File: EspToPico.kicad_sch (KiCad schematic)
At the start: 16 parts, among them J1 Conn_01x20_Pin, J2 Conn_01x20_Pin, J3 USB_C_Receptacle_USB2.0_16P, U1 ESP32-WROOM-E, U2 AP2112K-3.3, U3 TPD3E001DRLR, U4 MCP2200-I-MQ, Y1 CSTNE12M0GH5L000R0

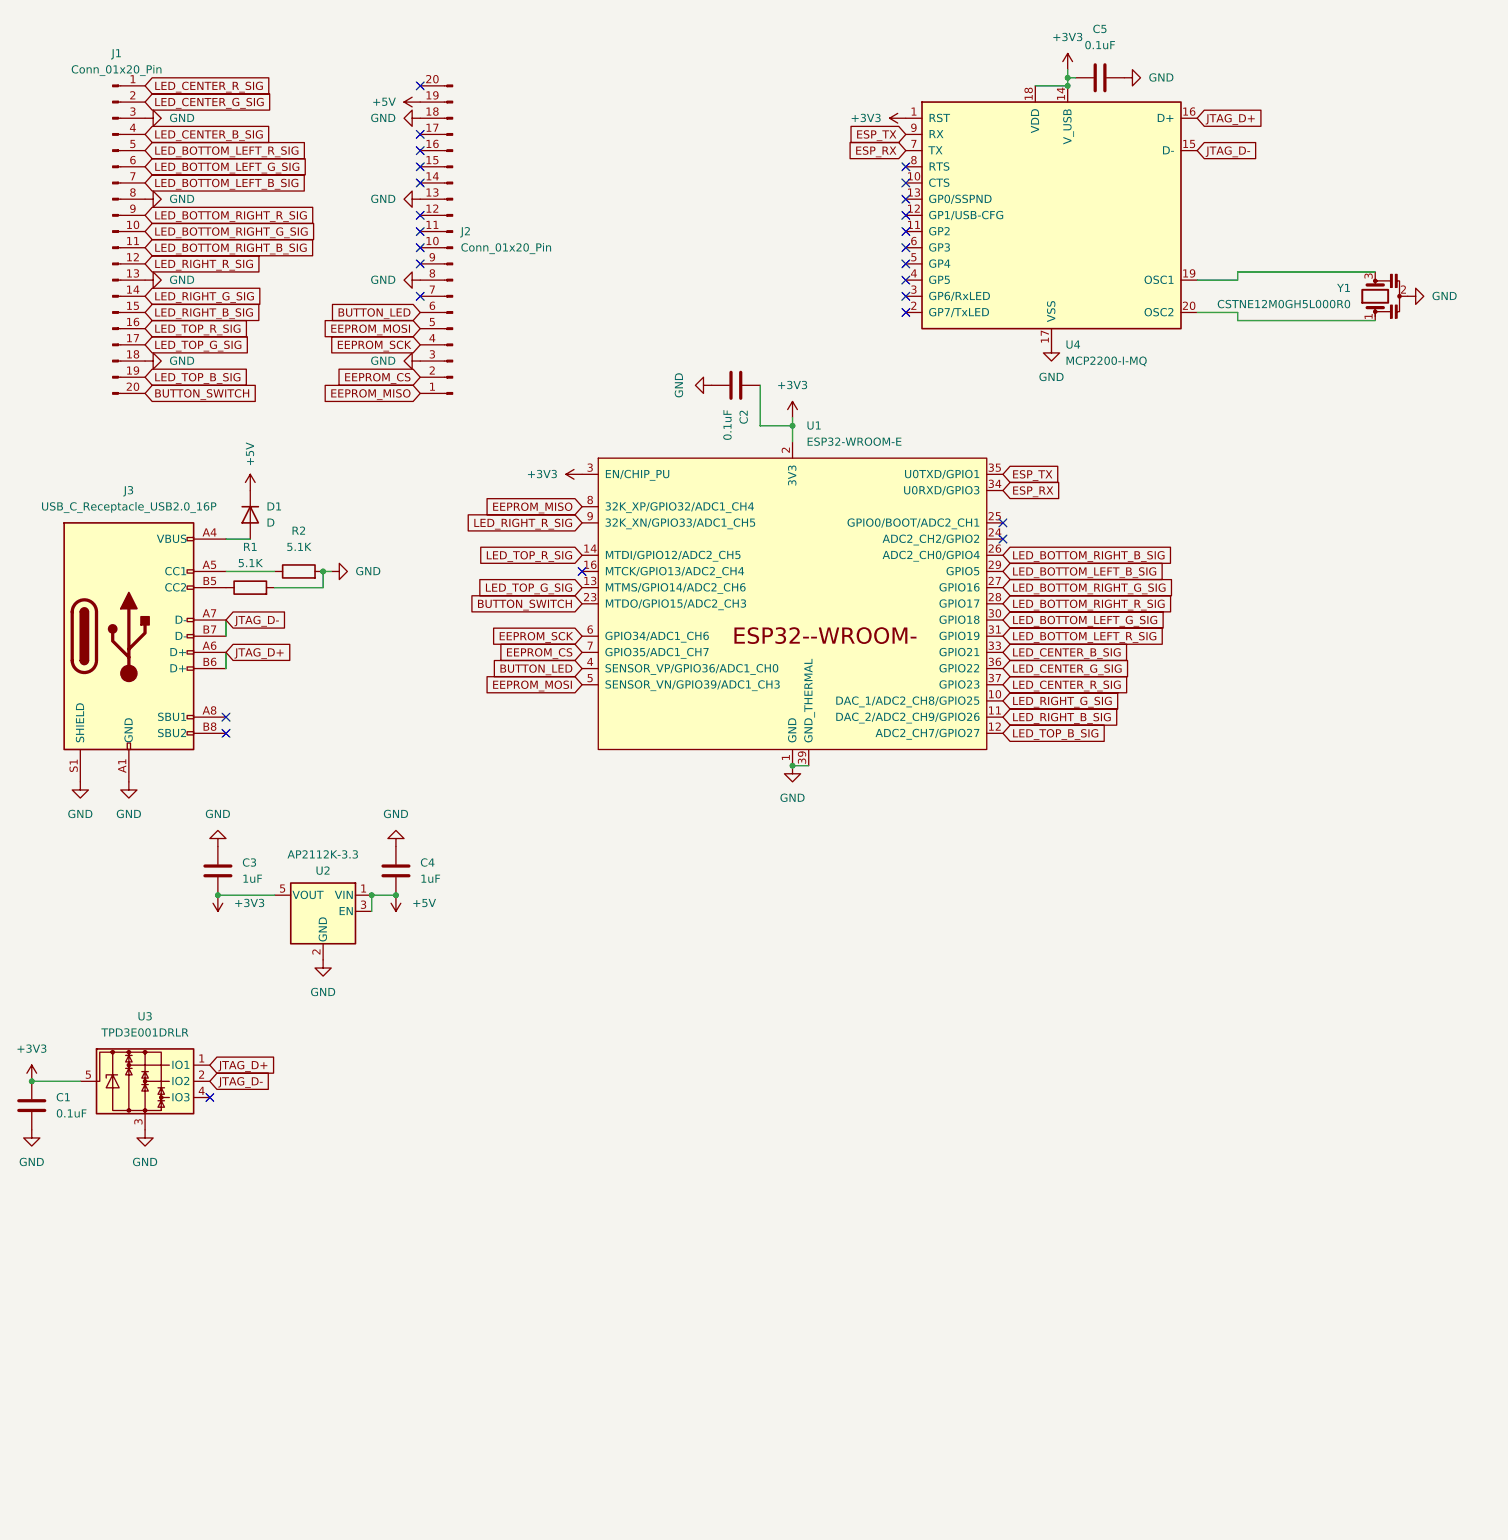
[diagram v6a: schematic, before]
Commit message: Reversed button switch and LED pins since the original LED pin is input only
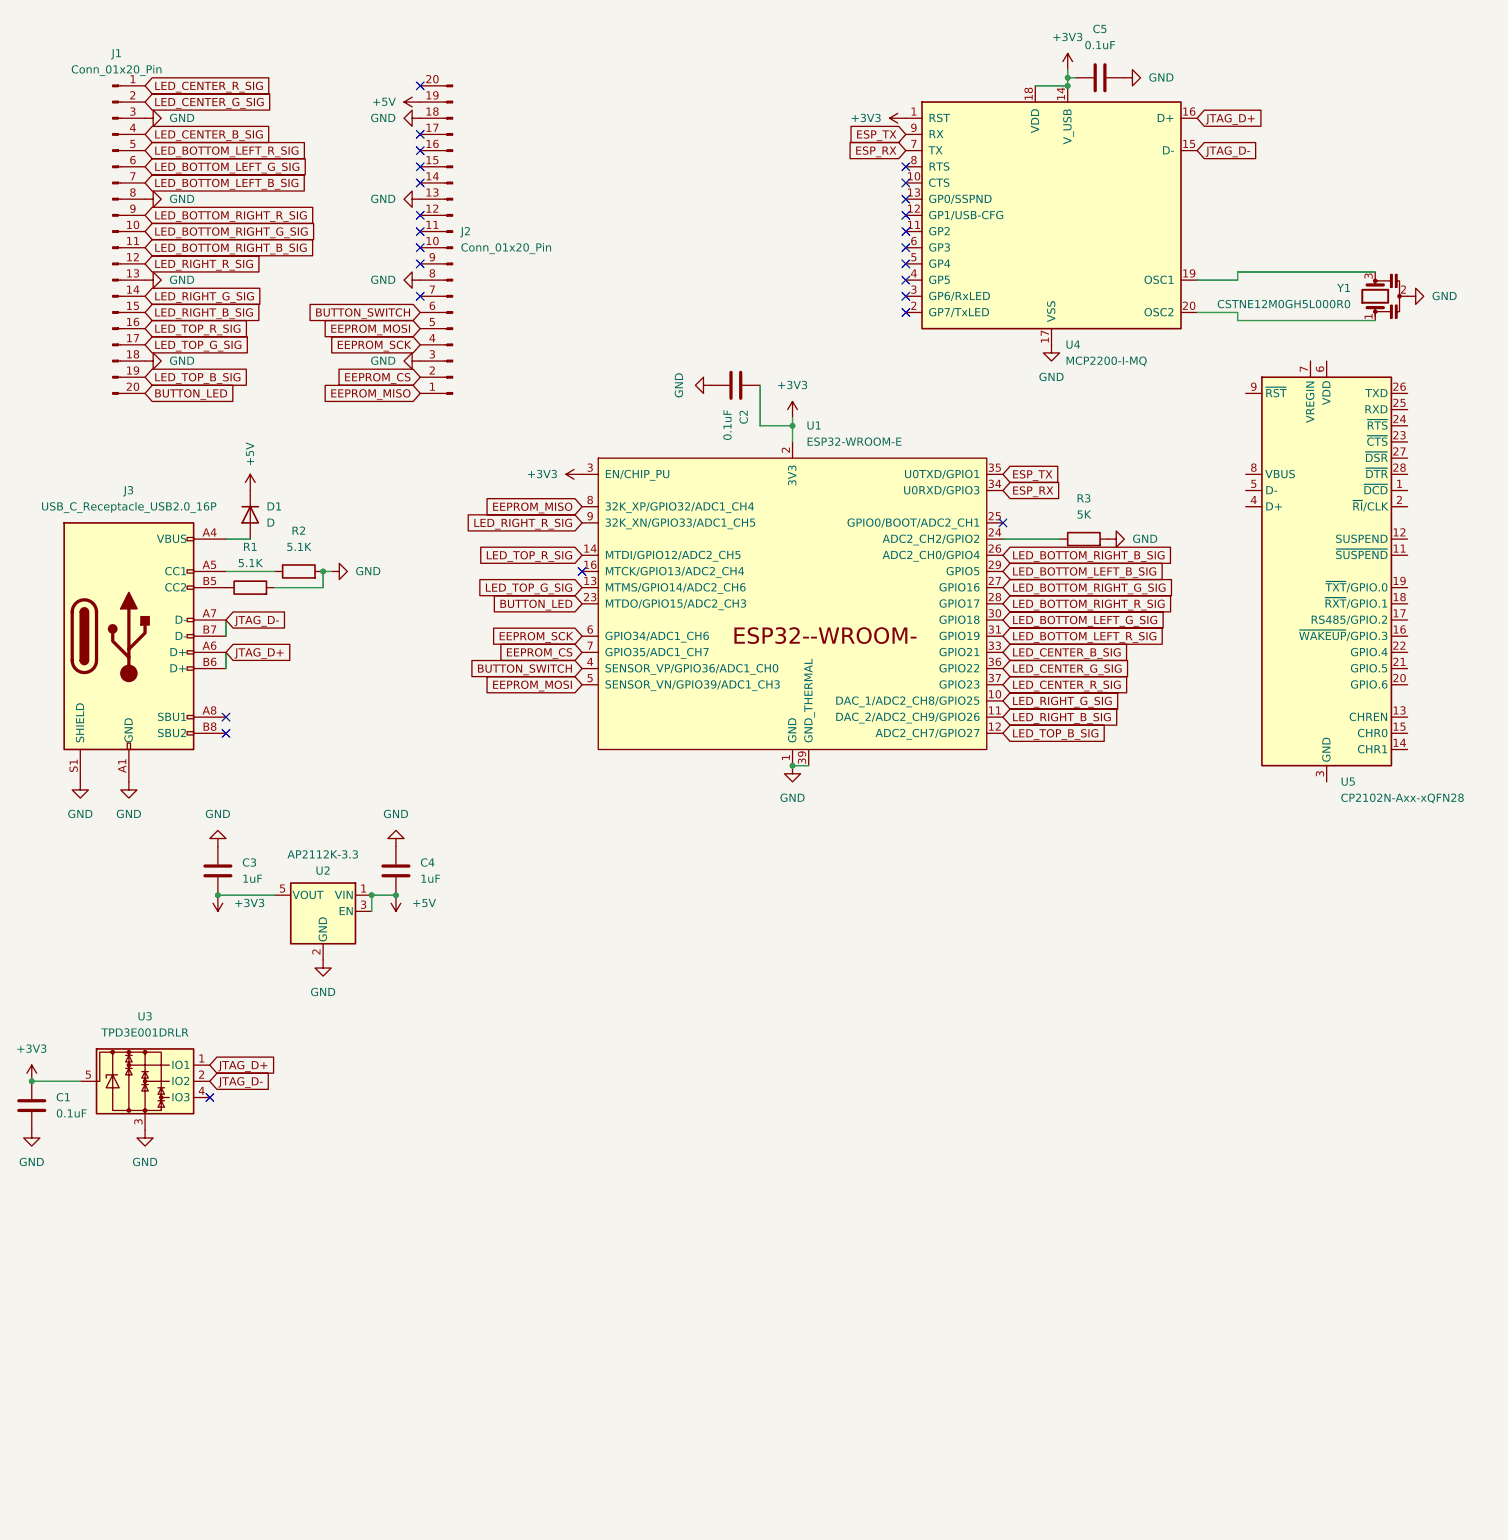
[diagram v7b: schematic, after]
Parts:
- added R3: 5K, Resistor_SMD:R_0402_1005Metric, symbol Device:R
- added U5: CP2102N-Axx-xQFN28, Package_DFN_QFN:QFN-28-1EP_5x5mm_P0.5mm_EP3.35x3.35mm, symbol Interface_USB:CP2102N-Axx-xQFN28
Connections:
- net BUTTON_LED: now also J1.20 (Pin_20), U1.23 (MTDO/GPIO15/ADC2_CH3); no longer J2.6 (Pin_6), U1.4 (SENSOR_VP/GPIO36/ADC1_CH0)
- net BUTTON_SWITCH: now also J2.6 (Pin_6), U1.4 (SENSOR_VP/GPIO36/ADC1_CH0); no longer J1.20 (Pin_20), U1.23 (MTDO/GPIO15/ADC2_CH3)
- net GND: now also R3.2
- net at U1.24 (ADC2_CH2/GPIO2): now also R3.1
- new net: U5.29 (GND), U5.3 (GND)
- no-connect marks 26 -> 25
